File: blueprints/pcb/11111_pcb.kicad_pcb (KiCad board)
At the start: 2 copper layers, 309.8 x 111.2 mm, 133 parts, among them J1 TRRS_MJ-4PP-9, J2 TRRS_MJ-4PP-9, SW1 SW_Push, SW10 SW_Push, SW11 SW_Push, SW12 SW_Push, SW13 SW_Push, SW14 SW_Push, SW15 SW_Push, SW16 SW_Push, SW17 SW_Push, SW18 SW_Push, SW19 SW_Push, SW2 SW_Push, SW20 SW_Push, SW21 SW_Push, SW22 SW_Push, SW23 SW_Push, SW24 SW_Push, SW25 SW_Push, SW26 SW_Push, SW27 SW_Push, SW28 SW_Push, SW29 SW_Push, SW3 SW_Push, SW30 SW_Push, SW31 SW_Push, SW32 SW_Push, SW33 SW_Push, SW34 SW_Push, SW35 SW_Push, SW36 SW_Push, SW37 SW_Push, SW38 SW_Push, SW39 SW_Push, SW4 SW_Push, SW40 SW_Push, SW41 SW_Push, SW42 SW_Push, SW43 SW_Push, SW44 SW_Push, SW45 SW_Push, SW46 SW_Push, SW47 SW_Push, SW48 SW_Push, SW49 SW_Push, SW5 SW_Push, SW50 SW_Push, SW51 SW_Push, SW52 SW_Push, SW53 SW_Push, SW54 SW_Push, SW55 SW_Push, SW56 SW_Push, SW57 SW_Push, SW58 SW_Push, SW59 SW_Push, SW6 SW_Push, SW60 SW_Push, SW61 SW_Push, SW62 SW_Push, SW63 SW_Push, SW64 SW_Push, SW7 SW_Push, SW8 SW_Push, SW9 SW_Push, U1 Pico, U2 Pico

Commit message: modify PCB and plates
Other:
- outline, holes or cut-outs redrawn
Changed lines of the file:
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@@
   (gr_line (start 192.84 131.48) (end 192.878025 25.396)
     (stroke (width 0.1) (type default)) (layer "Edge.Cuts"))
-  (gr_rect (start 35.5 111.76) (end 53.3 121.9)
+  (gr_rect (start 37.4 111.76) (end 54 121.9)
     (stroke (width 0.1) (type default)) (fill none) (layer "Edge.Cuts"))
   (gr_line (start 177.843949 25.396051) (end 177.843949 131.38)
@@
   (segment (start 269.995 121.88) (end 269.975 121.86) (width 0.25) (layer "F.Cu") (net 132))
   (via (at 269.995 121.88) (size 0.8) (drill 0.4) (layers "F.Cu" "B.Cu") (net 132))
+  (zone (net 74) (net_name "GND") (layers "F&B.Cu") (hatch edge 0.5)
+    (priority 1)
+    (connect_pads (clearance 0.508))
+    (min_thickness 0.25) (filled_areas_thickness no)
+    (fill yes (thermal_gap 0.5) (thermal_bridge_width 0.5))
+    (polygon
+      (pts
+        (xy 30.48 22.86)
+        (xy 177.8 22.86)
+        (xy 177.8 134.62)
+        (xy 30.48 134.62)
+      )
+    )
+  )
   (zone (net 113) (net_name "GNDA") (layers "F&B.Cu") (hatch edge 0.5)
     (connect_pads (clearance 0.508))
@@
     (polygon
       (pts
-        (xy 193.04 30.48)
-        (xy 335.28 30.48)
-        (xy 335.28 129.54)
-        (xy 193.04 129.54)
+        (xy 193.04 22.86)
+        (xy 340.36 22.86)
+        (xy 340.36 134.62)
+        (xy 193.04 134.62)
       )
     )
-  )
-  (zone (net 74) (net_name "GND") (layers "F&B.Cu") (hatch edge 0.5)
-    (priority 2)
-    (connect_pads (clearance 0.508))
-    (min_thickness 0.25) (filled_areas_thickness no)
-    (fill yes (thermal_gap 0.5) (thermal_bridge_width 0.5))
-    (polygon
-      (pts
-        (xy 35.56 30.48)
-        (xy 35.56 129.54)
-        (xy 177.8 129.54)
-        (xy 177.8 30.48)
-      )
-    )

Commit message: fix
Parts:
- added REF**: m3_Spacer_Hole_hex, keyboard_parts:m3_Spacer_Hole_hex, F.Cu at (186.4, 25.7)
- added REF**: m3_Spacer_Hole_hex, keyboard_parts:m3_Spacer_Hole_hex, F.Cu at (48.3, 85.8)
- added REF**: m3_Spacer_Hole_hex, keyboard_parts:m3_Spacer_Hole_hex, F.Cu at (265.5, 126.7)
- added REF**: m3_Spacer_Hole_hex, keyboard_parts:m3_Spacer_Hole_hex, F.Cu at (85.4, 126.6)
- added REF**: m3_Spacer_Hole_hex, keyboard_parts:m3_Spacer_Hole_hex, F.Cu at (322.0, 25.7)
- added REF**: m3_Spacer_Hole_hex, keyboard_parts:m3_Spacer_Hole_hex, F.Cu at (186.4, 126.7)
- added REF**: m3_Spacer_Hole_hex, keyboard_parts:m3_Spacer_Hole_hex, F.Cu at (164.4, 126.7)
- added REF**: m3_Spacer_Hole_hex, keyboard_parts:m3_Spacer_Hole_hex, F.Cu at (164.4, 25.7)
- added REF**: m3_Spacer_Hole_hex, keyboard_parts:m3_Spacer_Hole_hex, F.Cu at (302.5, 85.8)
- added REF**: m3_Spacer_Hole_hex, keyboard_parts:m3_Spacer_Hole_hex, F.Cu at (28.8, 25.7)
- moved SW26 12.8 mm to (273.9, 57.1)
- moved SW27 12.8 mm to (292.9, 57.1)
- moved SW28 12.8 mm to (312.0, 57.1)
- moved SW40 12.8 mm to (273.9, 76.1)
- moved SW41 12.8 mm to (292.9, 76.1)
- moved SW42 12.8 mm to (312.0, 76.1)
- moved SW54 12.8 mm to (273.9, 95.2)
- moved SW55 12.8 mm to (292.9, 95.2)
- moved SW56 12.8 mm to (312.0, 95.2)
- moved D11 12.8 mm to (255.7, 43.1)
- moved D12 12.8 mm to (274.7, 43.1)
- moved D14 12.8 mm to (312.8, 43.1)
- moved D25 12.8 mm to (255.7, 62.5)
- moved D26 12.8 mm to (274.7, 62.5)
- moved D28 12.8 mm to (312.8, 62.5)
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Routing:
- net Col10: track 112.8 -> 110.0 mm
- net Col13: track 123.4 -> 121.2 mm, vias 3 -> 2
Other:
- board size 309.8 x 111.2 mm -> 304.9 x 111.2 mm

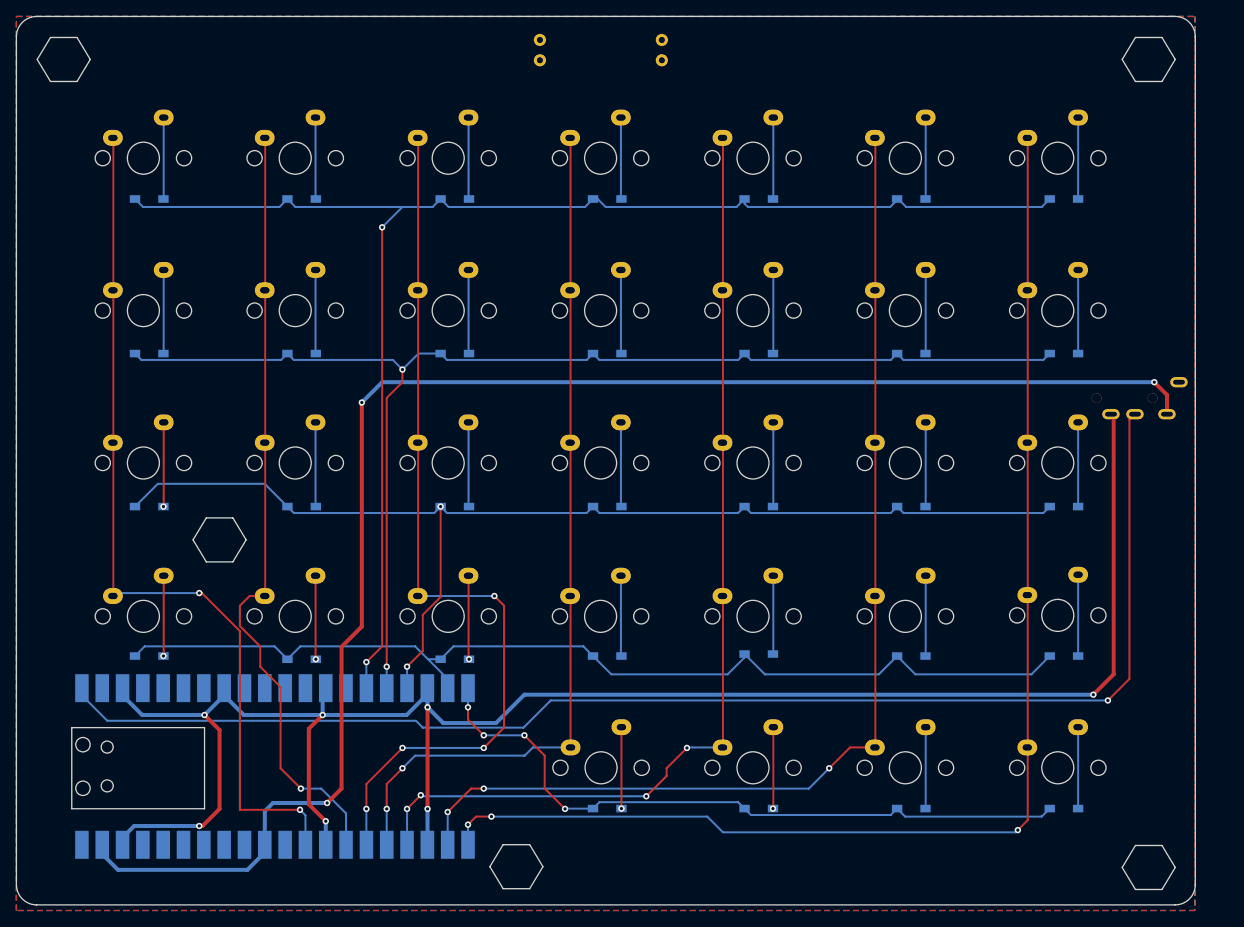
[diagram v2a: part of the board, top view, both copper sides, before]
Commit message: narrow left PCB
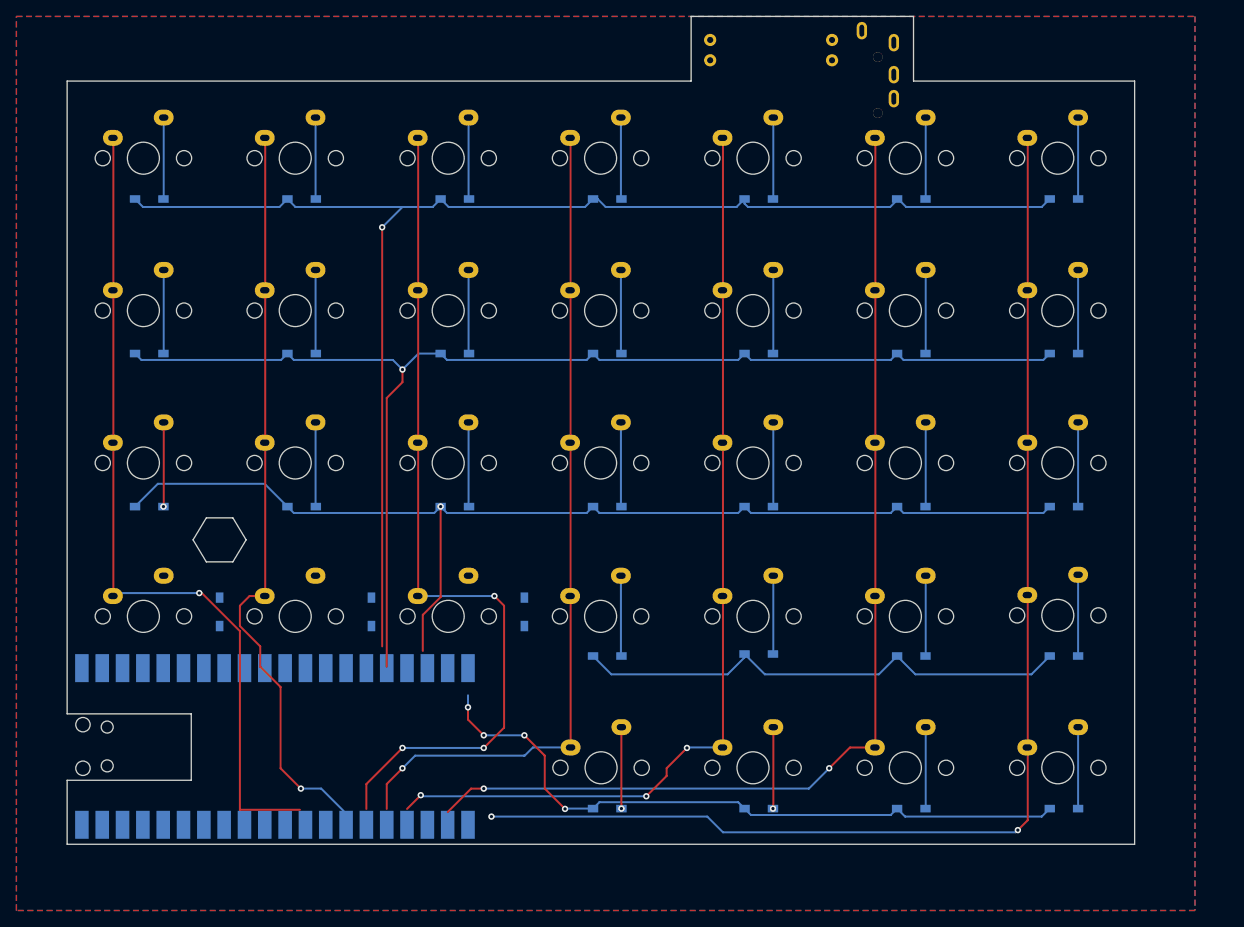
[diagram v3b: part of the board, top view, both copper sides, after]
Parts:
- removed the REF** at (85.4, 126.6)
- removed the REF** at (164.4, 126.7)
- removed the REF** at (164.4, 25.7)
- removed the REF** at (28.8, 25.7)
- moved J1 51.2 mm to (130.5, 27.9), turned to 180 degrees
- moved REF** 21.3 mm to (117.2, 20.3)
- moved D44 10.5 mm to (67.2, 94.7), turned to 90 degrees
- moved D45 10.5 mm to (86.4, 94.7), turned to 90 degrees
- moved D43 10.4 mm to (48.3, 94.7), turned to 90 degrees
- moved U1 2.50 mm to (55.2, 111.6)
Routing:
- net GND: track 228.1 -> 0.00 mm, vias 7 -> 0
- net VCC: track 194.1 -> 0.00 mm, vias 3 -> 0
- net DataLeft: track 168.5 -> 0.00 mm, vias 1 -> 0
- net Row3: track 126.8 -> 63.2 mm
- net Net-(D45-A): track 10.5 -> 0.00 mm, vias 1 -> 0
- net Net-(D44-A): track 10.5 -> 0.00 mm, vias 1 -> 0
- net Net-(D43-A): track 10.1 -> 0.00 mm, vias 1 -> 0
- net Row0: track 186.4 -> 179.5 mm, vias 2 -> 1
- net Row2: track 145.3 -> 139.0 mm, vias 2 -> 1
- net Col6: track 158.8 -> 153.8 mm, vias 3 -> 2
- net Col0: track 108.9 -> 105.2 mm, vias 2 -> 1
- net Row1: track 160.8 -> 157.3 mm, vias 2 -> 1
- net Col4: track 123.1 -> 119.5 mm, vias 4 -> 3
- net Col3: track 107.9 -> 104.3 mm, vias 2 -> 1
- net Col2: track 110.7 -> 107.1 mm, vias 4 -> 3
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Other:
- board size 304.9 x 111.2 mm -> 298.5 x 111.2 mm
